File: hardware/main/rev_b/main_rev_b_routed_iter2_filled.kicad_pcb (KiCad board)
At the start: 4 copper layers, 140 x 100 mm, 165 parts, among them J1 USB-C USB2, J10 SWD, J2 ESC_CAN_POWER, J30 GNSS_UFL, J40 915MHz_ANT, Q30 2N7002, U1 USBLC6-2SC6, U10 RP2354B, U2 TLV62569DBVR, U20 ICM-42688-P, U21 LSM6DSO32TR, U22 LPS22DFTR, U3 TLV75528PDBVR, U30 LG77LICMD, U4 TLV75533PDBVR, U40 CC1121RHBR, U41 CC1190RGVR, U50 TCAN3413DR, U51 MCP2518FD-H/QBB, Y1 12MHz ABM8-272-T3, Y40 32MHz NT2016SA-32M-TEE3017A, Y50 40MHz ABM8G

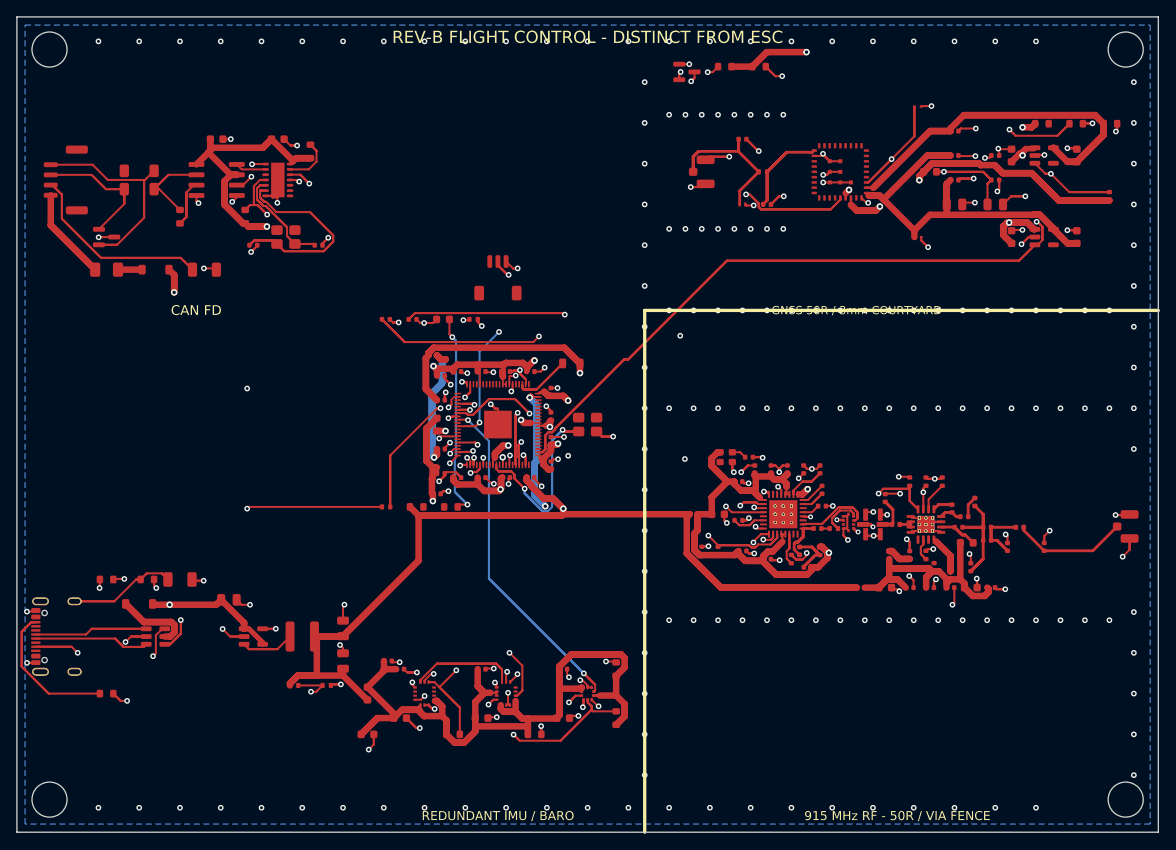
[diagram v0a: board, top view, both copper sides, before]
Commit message: route: continue Rev-B main routing without plane nets
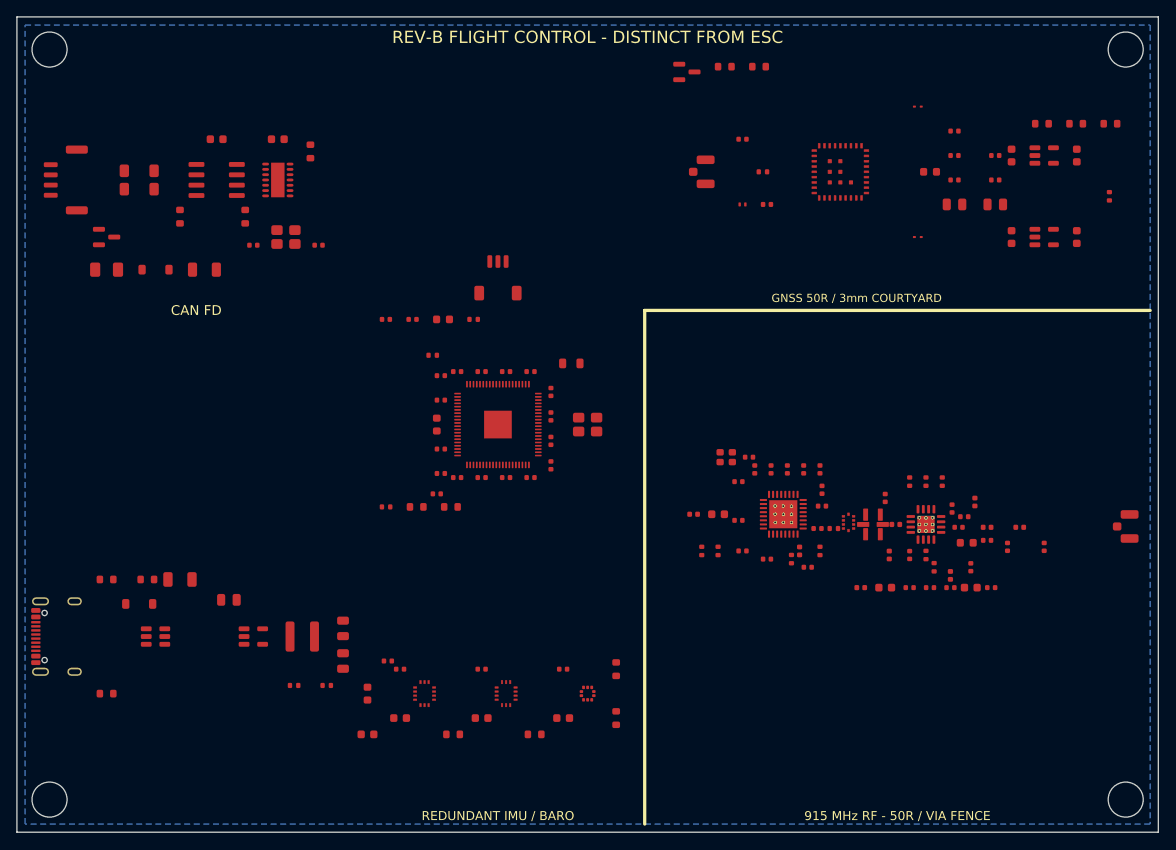
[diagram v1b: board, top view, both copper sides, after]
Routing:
- net /3V3: track 560.3 -> 0.00 mm, vias 10 -> 0
- net /SYS_5V: track 291.0 -> 0.00 mm, vias 4 -> 0
- net /GND: track 288.9 -> 0.00 mm, vias 265 -> 0
- net /CAN_INT: track 261.7 -> 0.00 mm, vias 2 -> 0
- net /GNSS_RESET_N: track 189.7 -> 0.00 mm, vias 4 -> 0
- net /GNSS_PWR_EN: track 178.7 -> 0.00 mm, vias 2 -> 0
- net /Redundant sensors/3V3_SENS: track 131.4 -> 0.00 mm
- net /PA_EN: track 122.2 -> 0.00 mm, vias 2 -> 0
- net /GNSS/GNSS_RESET_OD: track 112.4 -> 0.00 mm, vias 3 -> 0
- net /GNSS_TX: track 111.2 -> 0.00 mm, vias 3 -> 0
- net /915 MHz RF/VDD_CC112: track 108.8 -> 0.00 mm, vias 2 -> 0
- net /SENS_MISO: track 107.5 -> 0.00 mm, vias 3 -> 0
- net /RP2354B MCU/XIN: track 107.2 -> 0.00 mm, vias 3 -> 0
- net /BARO_SDA: track 101.6 -> 0.00 mm, vias 2 -> 0
- net /USB_DP: track 100.8 -> 0.00 mm, vias 3 -> 0
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
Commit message: route: preserve recovered Rev-B main checkpoint
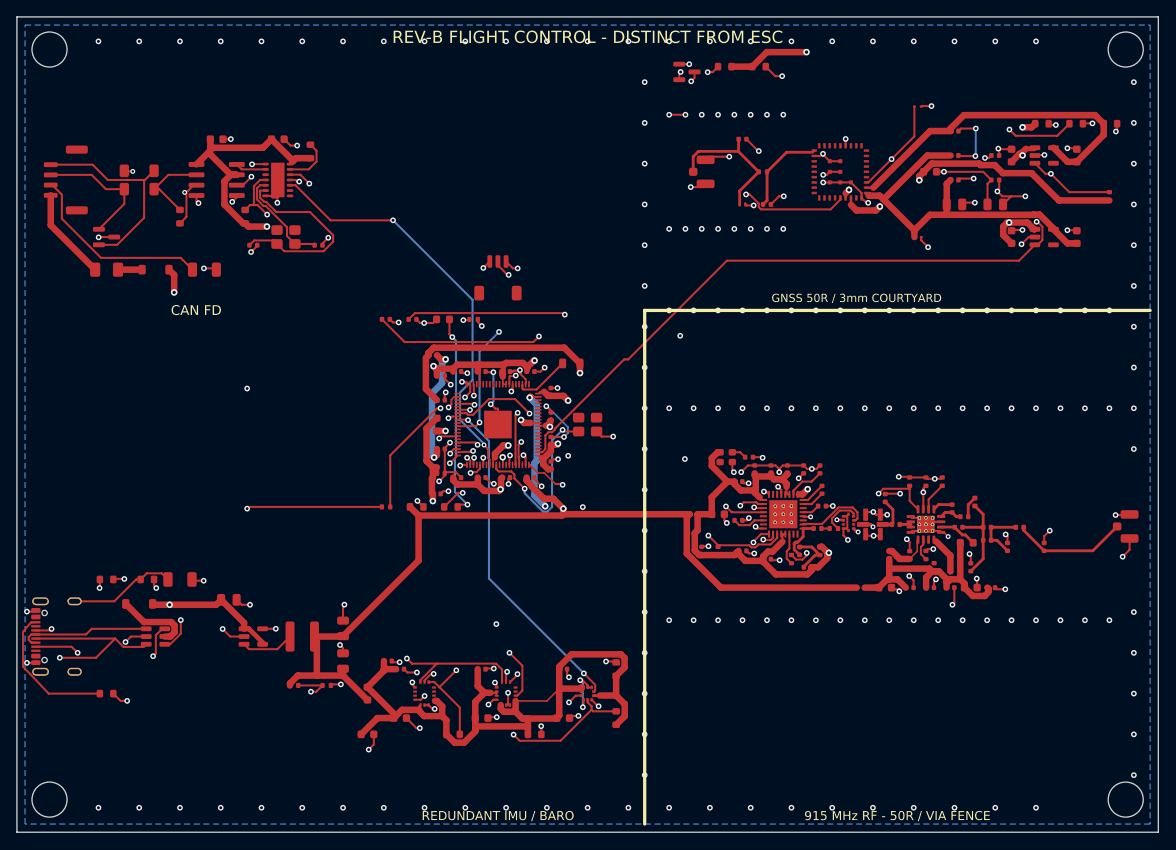
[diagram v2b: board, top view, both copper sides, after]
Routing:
- net /GND: track 0.00 -> 1344.8 mm, vias 0 -> 266
- net /3V3: track 0.00 -> 331.6 mm, vias 0 -> 10
- net /SYS_5V: track 0.00 -> 195.0 mm, vias 0 -> 4
- net /CAN_INT: track 0.00 -> 137.7 mm, vias 0 -> 2
- net /GNSS_RESET_N: track 0.00 -> 126.4 mm, vias 0 -> 4
- net /Redundant sensors/3V3_SENS: track 0.00 -> 97.6 mm
- net /GNSS_PWR_EN: track 0.00 -> 93.5 mm, vias 0 -> 2
- net /GNSS/GNSS_RESET_OD: track 0.00 -> 86.9 mm, vias 0 -> 3
- net /915 MHz RF/VDD_CC112: track 0.00 -> 68.2 mm, vias 0 -> 2
- net /USB_DP: track 0.00 -> 66.7 mm, vias 0 -> 3
- net /PA_EN: track 0.00 -> 66.4 mm, vias 0 -> 2
- net /GNSS_TX: track 0.00 -> 63.7 mm, vias 0 -> 3
- net /SENS_MOSI: track 0.00 -> 62.1 mm, vias 0 -> 3
- net /BARO_SDA: track 0.00 -> 60.6 mm, vias 0 -> 2
- net /LNA_EN: track 0.00 -> 60.4 mm, vias 0 -> 2
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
